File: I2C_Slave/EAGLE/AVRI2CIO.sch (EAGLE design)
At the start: 39 parts, among them IC1 MEGA8-P

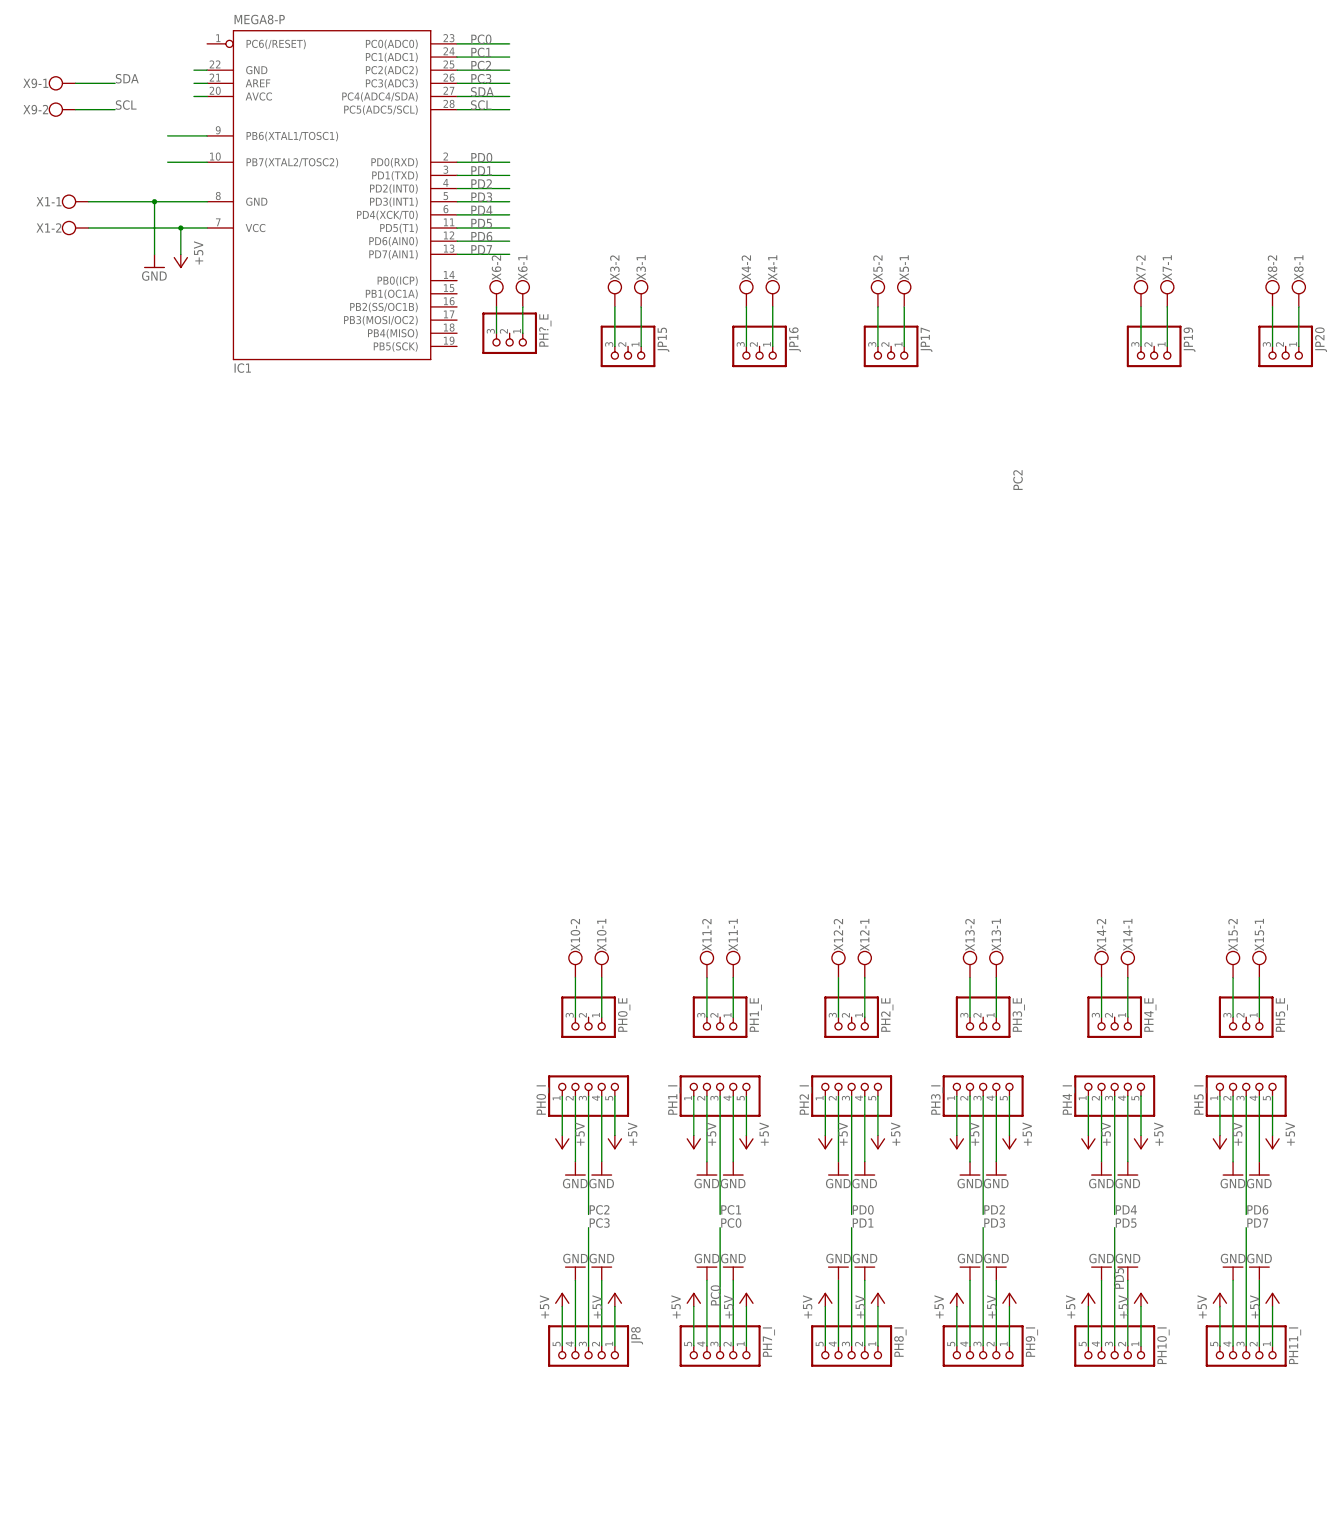
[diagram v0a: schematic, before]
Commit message: modify eagle item names
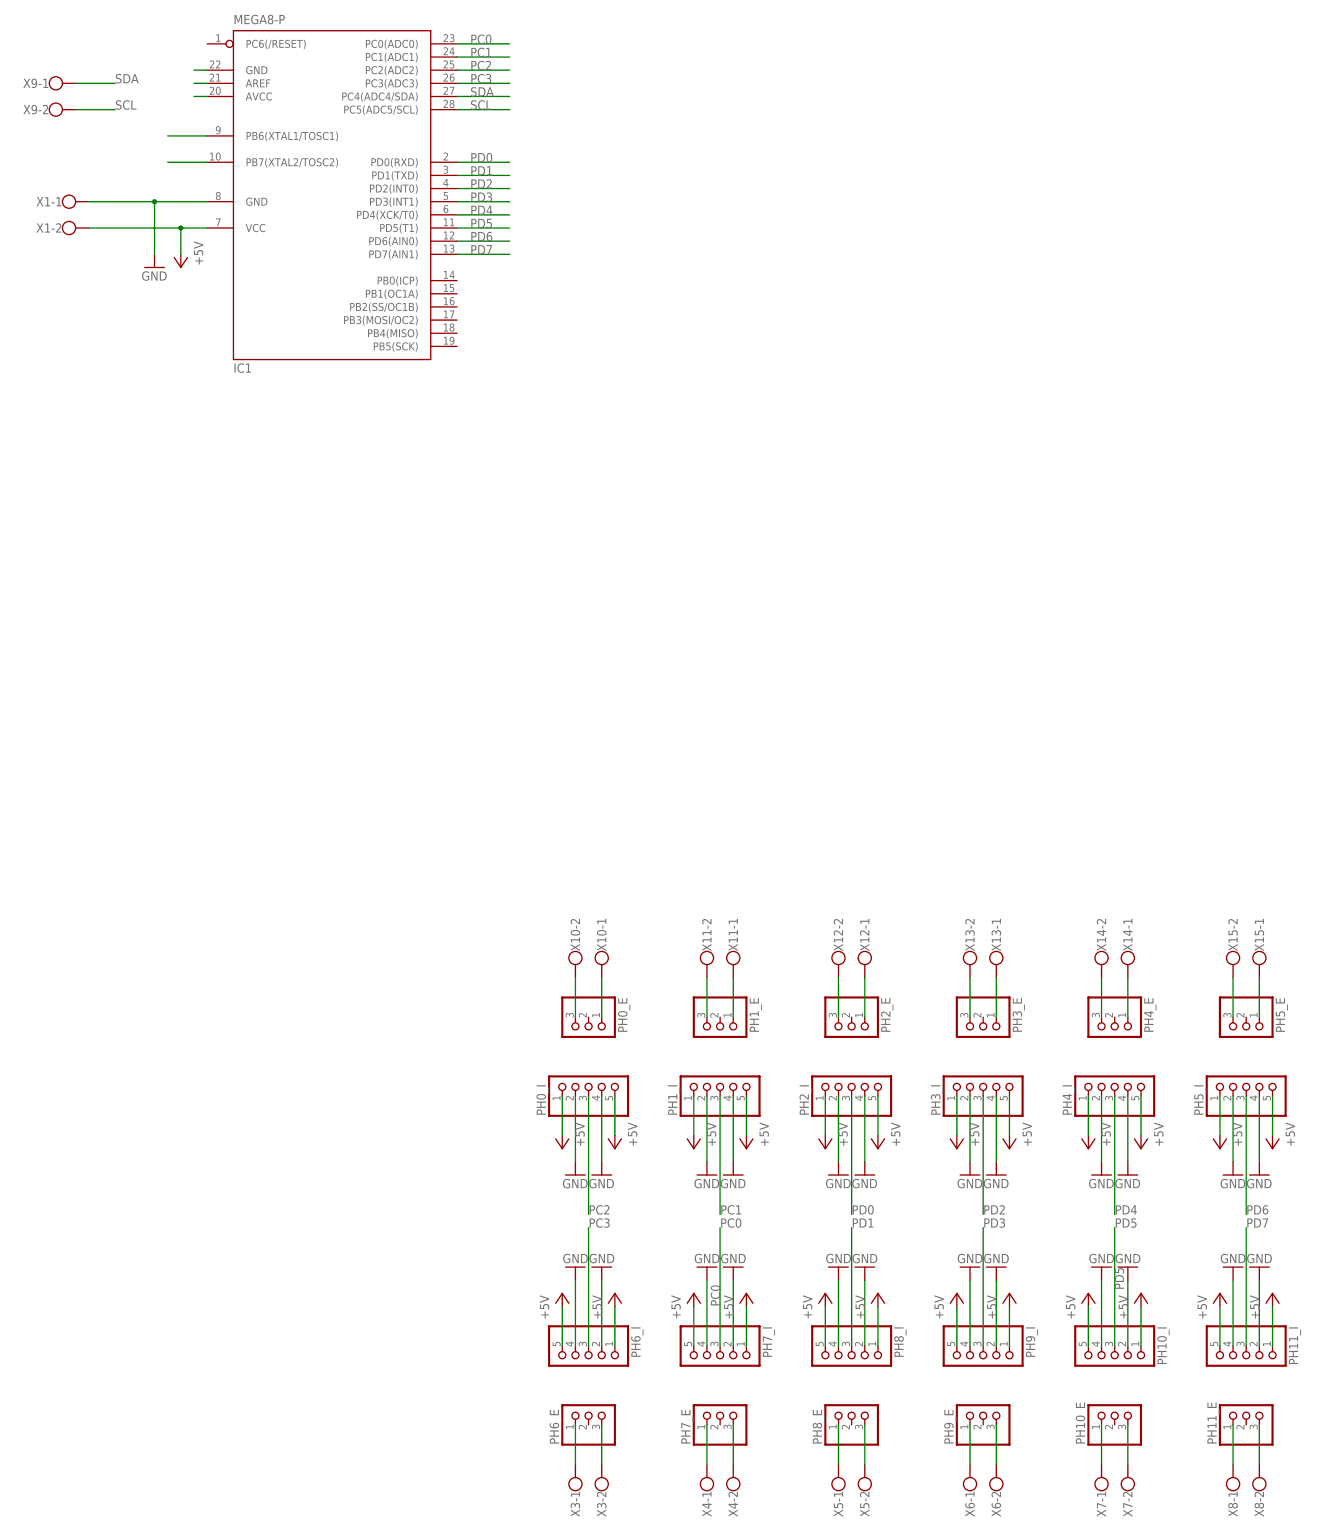
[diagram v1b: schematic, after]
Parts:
- removed JP15, JP16, JP17, JP19, JP20, PH?_E: (no value), pinhead:PINHD-1X3
- added PH10_E, PH11_E, PH6_E, PH7_E, PH8_E, PH9_E: (no value), pinhead:PINHD-1X3
- renumbered JP8 to PH6_I
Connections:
- net N$10: now also PH9_E.1; no longer PH?_E.1
- net N$11: now also PH10_E.3; no longer JP19.3
- net N$12: now also PH10_E.1; no longer JP19.1
- net N$13: now also PH11_E.3; no longer JP20.3
- net N$14: now also PH11_E.1; no longer JP20.1
- net N$3: now also PH6_E.3; no longer JP15.3
- net N$4: now also PH6_E.1; no longer JP15.1
- net N$5: now also PH7_E.3; no longer JP16.3
- net N$6: now also PH7_E.1; no longer JP16.1
- net N$7: now also PH8_E.3; no longer JP17.3
- net N$8: now also PH8_E.1; no longer JP17.1
- net N$9: now also PH9_E.3; no longer PH?_E.3
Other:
- moved on the sheet: X3-1, X3-2, X4-1, X4-2, X5-1, X5-2, X6-1, X6-2, X7-1, X7-2, X8-1, X8-2
